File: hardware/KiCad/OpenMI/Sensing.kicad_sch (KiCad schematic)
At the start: 60 parts, among them U10 MCS1802GS-05, U11 MCP6001T-OT, U12 MCP6567-SN, U14 MCP6561-OT, U2 INA381A2IDGS, U5 MCP6004-SL, U7 MCP6001T-OT

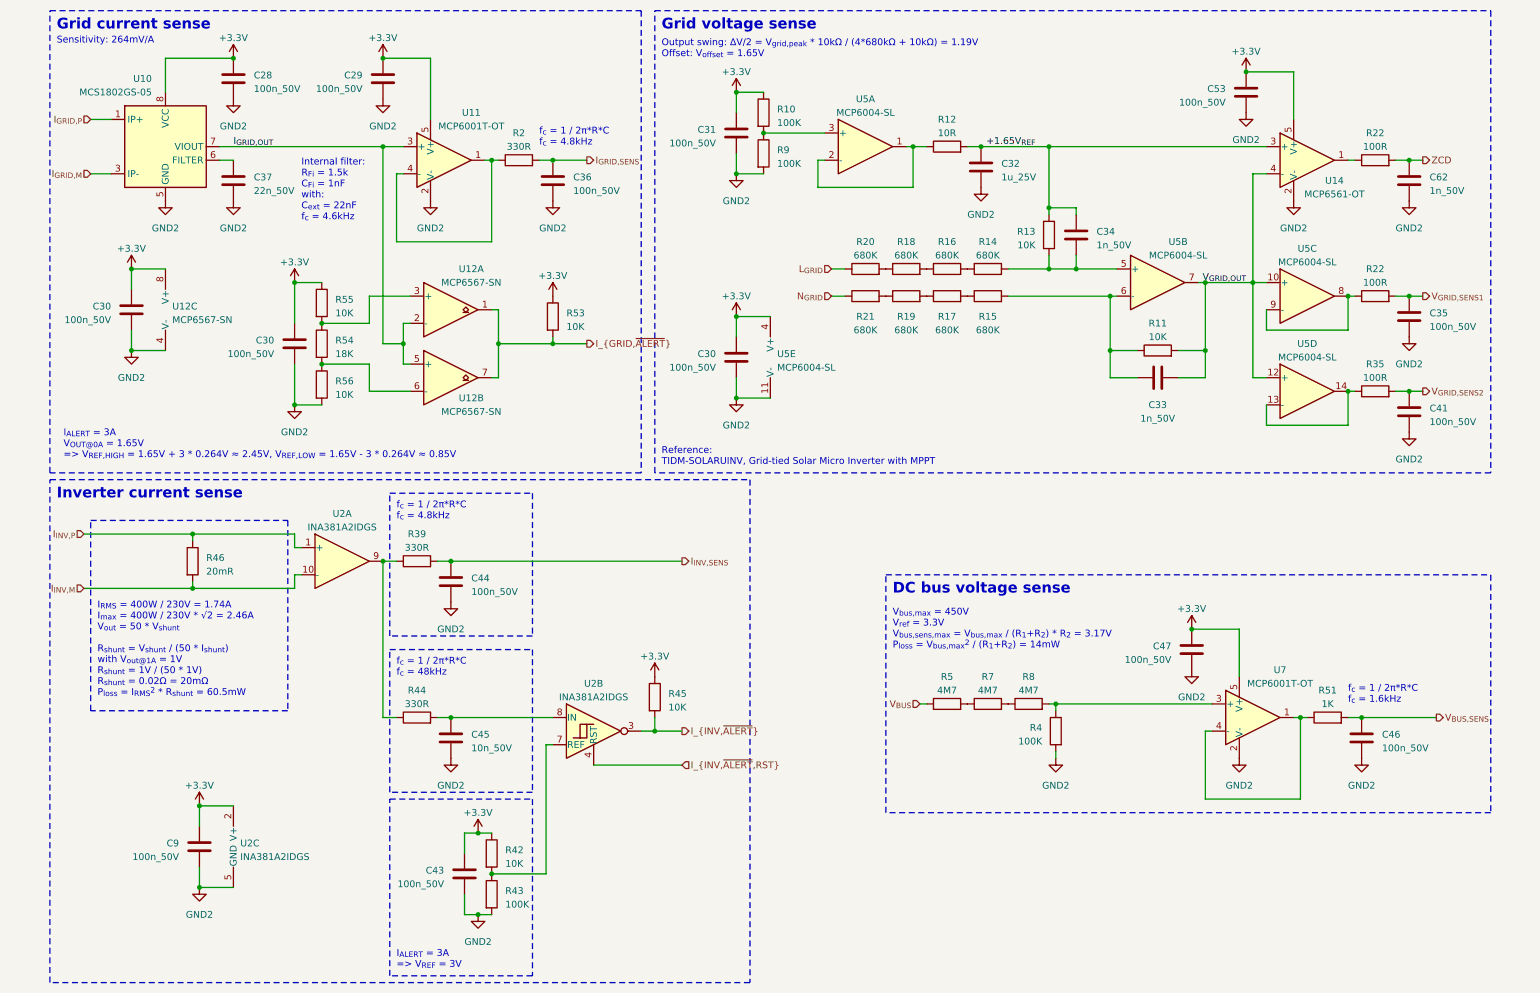
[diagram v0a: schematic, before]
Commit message: chore(hw): updates project to KiCad 8
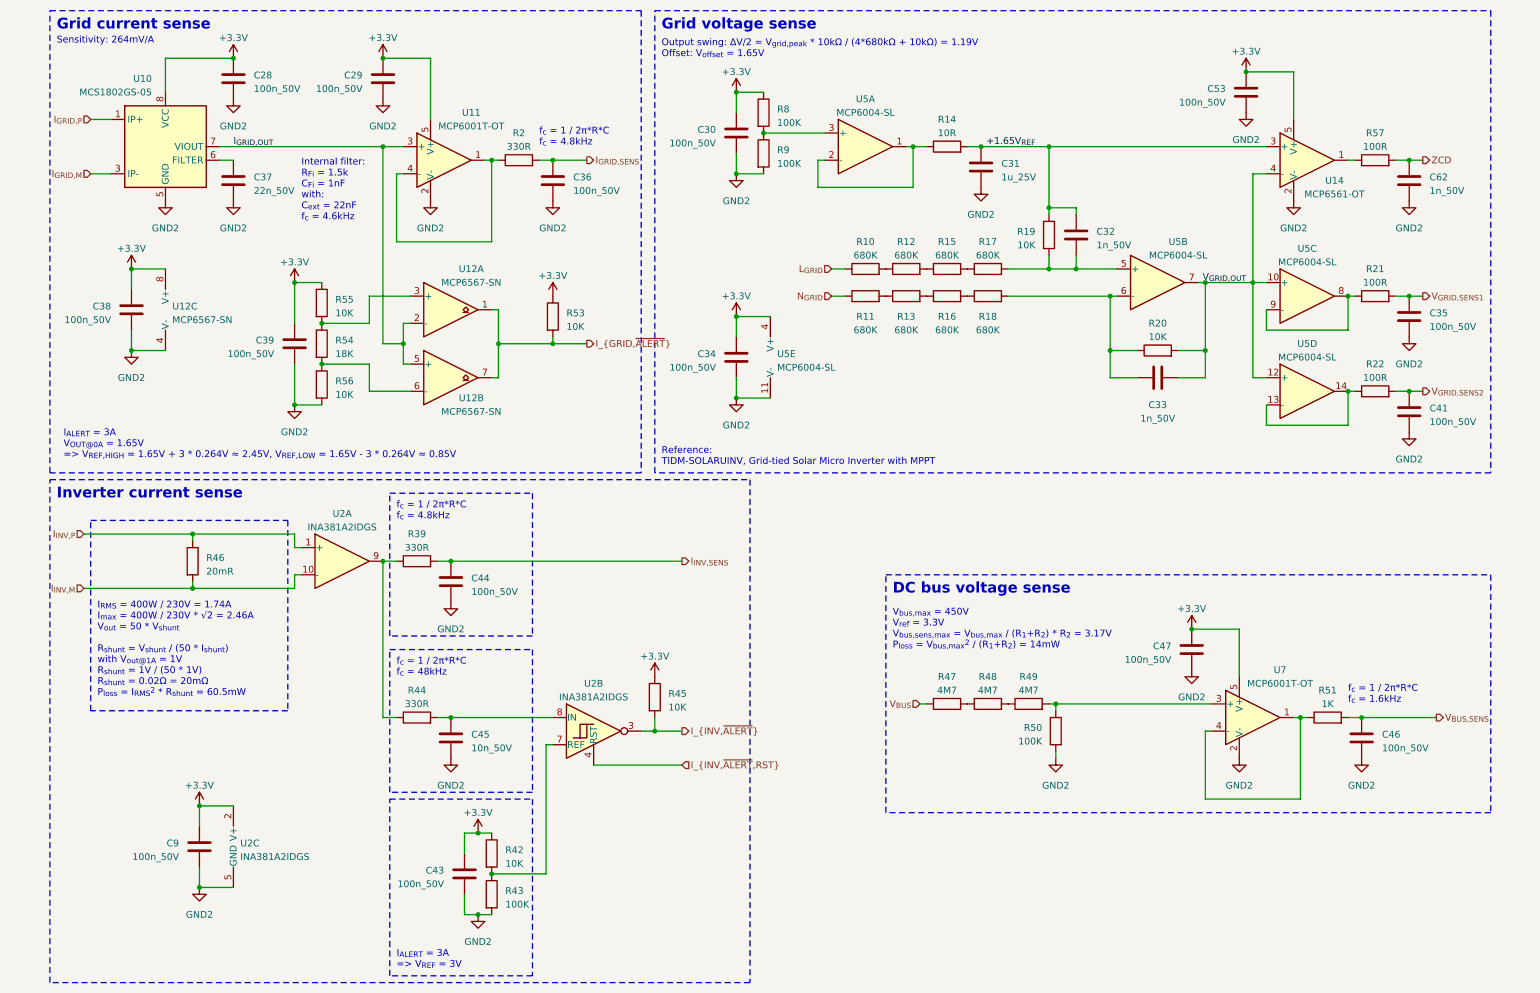
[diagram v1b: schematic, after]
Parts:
- renumbered C31 to C30, C32 to C31, C34 to C32, C30 to C34, C30 to C38, C30 to C39, R20 to R10, R21 to R11, R18 to R12, R19 to R13, R12 to R14, R16 to R15, R17 to R16, R14 to R17, R15 to R18, R13 to R19, R11 to R20, R22 to R21, R35 to R22, R5 to R47, R7 to R48, R8 to R49, R4 to R50, R22 to R57, R10 to R8
